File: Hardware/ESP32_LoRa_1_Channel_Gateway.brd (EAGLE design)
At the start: 25.4 x 45.7 mm, 86 parts, among them J3 USB, J4 QWIIC, J6 U.FL, Q1 MBT3904DW1T1, U1 3.3V, U2 CH340C, U3 ESP-WROOM-32NARROW, U4 RFM95W

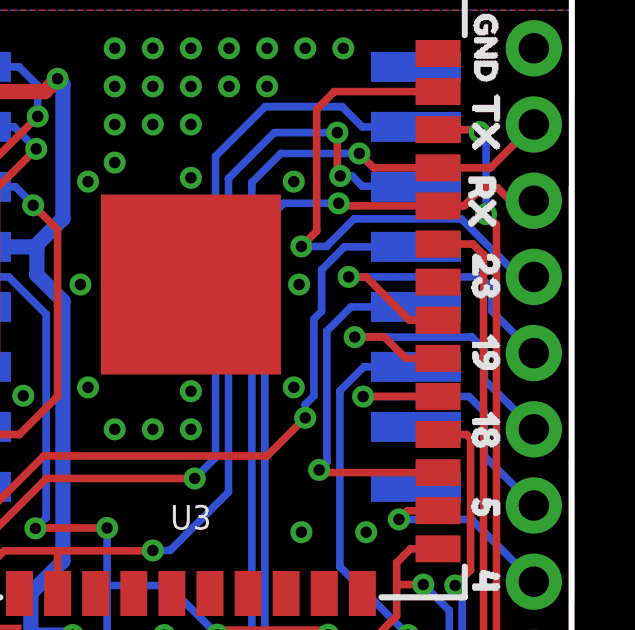
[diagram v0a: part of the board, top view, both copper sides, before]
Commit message: Moved CC atribution
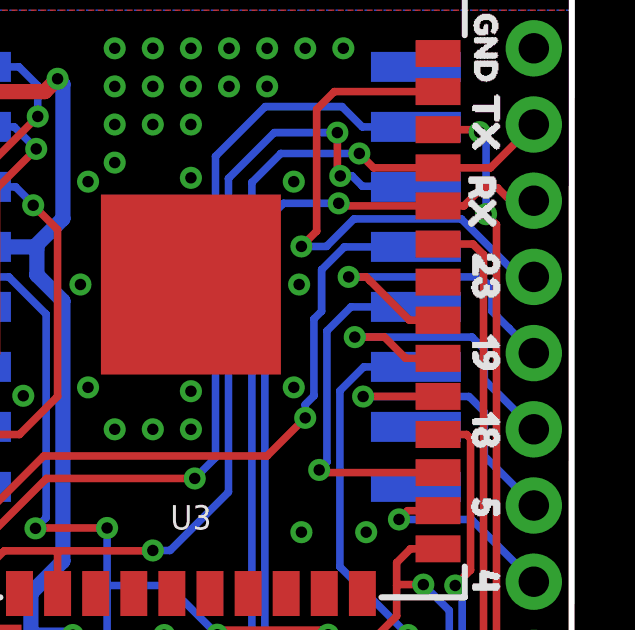
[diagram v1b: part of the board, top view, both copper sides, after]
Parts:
- moved FRAME1 7.83 mm to (-4.95, -9.91)
- moved LOGO2 7.65 mm to (6.48, -13.0)
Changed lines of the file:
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@@
 <hole x="1.27" y="17.78" drill="1.016"/>
 <text x="2.032" y="0.381" size="1.27" layer="16" font="vector" ratio="15" rot="MR0">v1</text>
-<text x="29.21" y="-7.62" size="1.778" layer="51" font="vector" ratio="15">Jim Lindblom</text>
-<text x="29.21" y="-11.43" size="1.778" layer="51" font="vector" ratio="15">Owen Lyke</text>
+<text x="22.479" y="-10.033" size="1.778" layer="51" font="vector" ratio="15">Jim Lindblom</text>
+<text x="22.352" y="-12.954" size="1.778" layer="51" font="vector" ratio="15">Owen Lyke</text>
 <dimension x1="27.94" y1="0" x2="27.94" y2="45.72" x3="30.48" y3="22.86" textsize="1.778" textratio="15" layer="47" unit="inch"/>
 <dimension x1="0" y1="48.26" x2="25.4" y2="48.26" x3="12.7" y3="50.8" textsize="1.778" textratio="15" layer="47" unit="inch"/>
@@
 <attribute name="VALUE" x="9.144" y="18.034" size="0.6096" layer="27" font="vector" ratio="20" rot="R180" align="top-center"/>
 </element>
-<element name="FRAME1" library="SparkFun-Aesthetics" package="CREATIVE_COMMONS" value="FRAME-LETTER" x="2.54" y="-7.62"/>
+<element name="FRAME1" library="SparkFun-Aesthetics" package="CREATIVE_COMMONS" value="FRAME-LETTER" x="-4.953" y="-9.906"/>
 <element name="Q1" library="esp32-thing-temp" package="SC70-6" value="MBT3904DW1T1" x="17.78" y="16.51" smashed="yes" rot="R90">
 <attribute name="NAME" x="16.383" y="16.51" size="0.6096" layer="25" font="vector" ratio="20" rot="R90" align="bottom-center"/>
@@
 <element name="U$45" library="buzzard_labels" package="ESP32_LORA_1#CH_GATEWAY23" value="" x="24.003" y="8.763" rot="MR0"/>
 <element name="LOGO1" library="SparkFun-Aesthetics" package="OSHW-LOGO-M" value="OSHW-LOGOM" x="22.606" y="2.54" rot="MR0"/>
-<element name="LOGO2" library="SparkFun-Aesthetics" package="REVISION" value="REVISION" x="13.97" y="-11.43"/>
+<element name="LOGO2" library="SparkFun-Aesthetics" package="REVISION" value="REVISION" x="6.477" y="-12.954"/>
 <element name="FD1" library="SparkFun-Aesthetics" package="FIDUCIAL-1X2" value="FIDUCIAL1X2" x="24.13" y="44.45"/>
 <element name="FD2" library="SparkFun-Aesthetics" package="FIDUCIAL-1X2" value="FIDUCIAL1X2" x="24.13" y="44.45" rot="MR0"/>
@@
 <wire x1="20.938" y1="29.036" x2="19.986" y2="29.036" width="0.254" layer="1"/>
 <wire x1="18.542" y1="30.48" x2="17.9578" y2="30.48" width="0.254" layer="1"/>
-<wire x1="19.986" y1="29.036" x2="18.542" y2="30.48" width="0.254" layer="1"/>
+<wire x1="19.986" y1="29.036" x2="18.669" y2="30.353" width="0.254" layer="1"/>
+<wire x1="18.669" y1="30.353" x2="18.542" y2="30.48" width="0.254" layer="1"/>
 <wire x1="22.352" y1="30.48" x2="22.733" y2="30.099" width="0.254" layer="16"/>
 <wire x1="22.733" y1="30.099" x2="22.733" y2="29.337" width="0.254" layer="16"/>
 <wire x1="17.9578" y1="30.48" x2="22.352" y2="30.48" width="0.254" layer="16"/>
-<wire x1="22.733" y1="29.337" x2="24.13" y2="27.94" width="0.254" layer="16"/>
+<wire x1="22.733" y1="29.337" x2="23.3045" y2="28.7655" width="0.254" layer="16"/>
+<wire x1="23.3045" y1="28.7655" x2="24.13" y2="27.94" width="0.254" layer="16"/>
 </signal>
 <signal name="IO18">

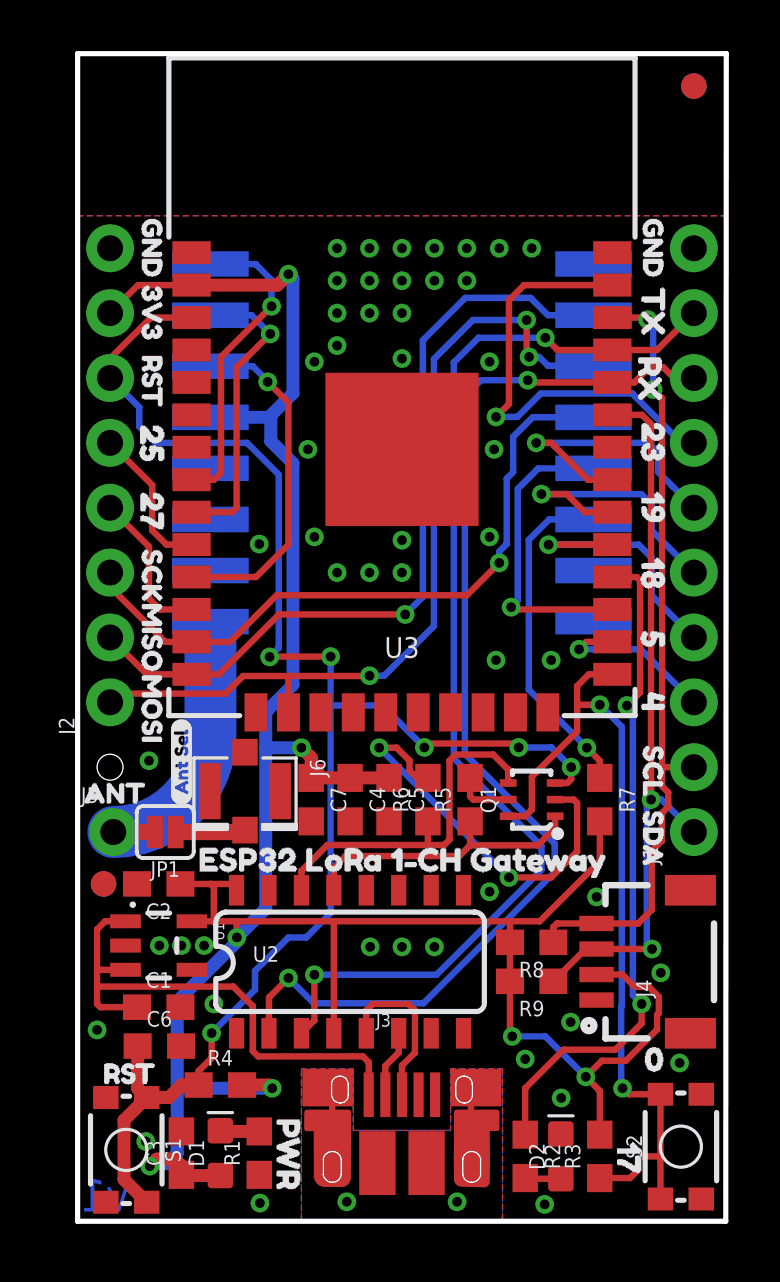
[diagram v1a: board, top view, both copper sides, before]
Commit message: Moved LEDs and silk
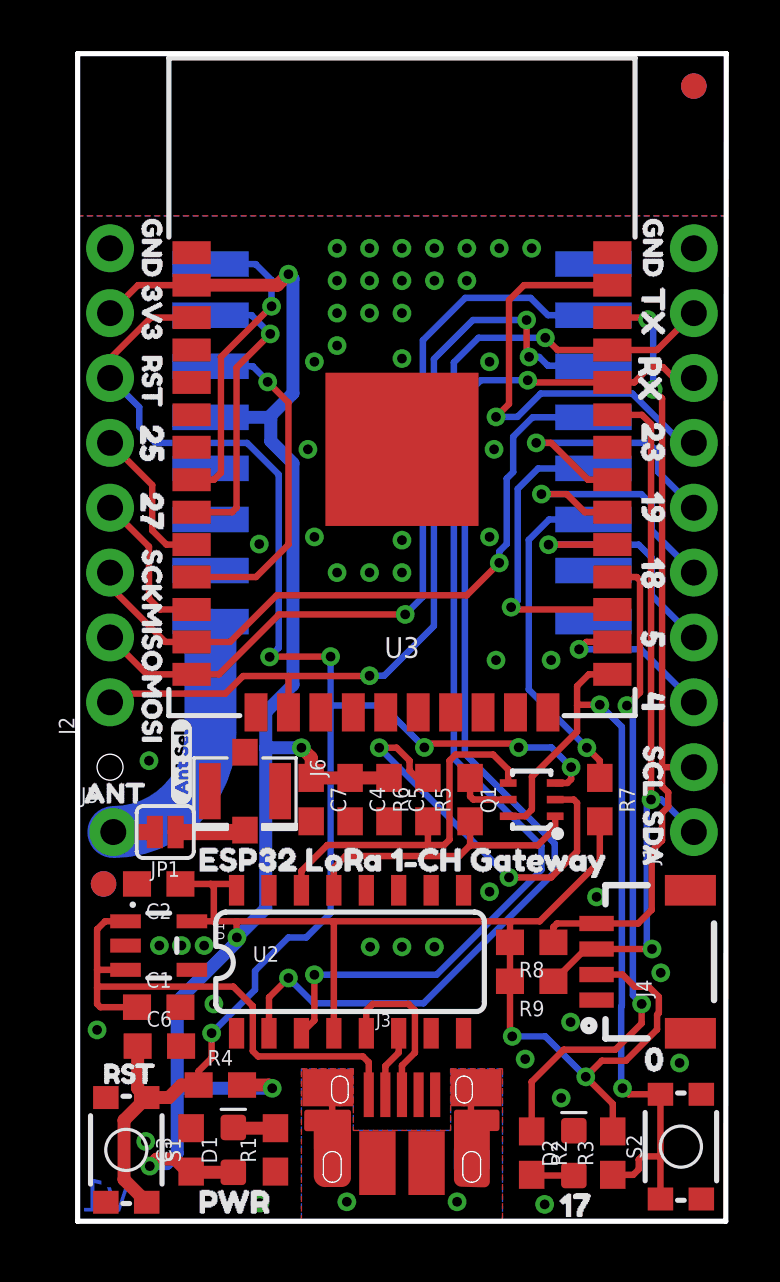
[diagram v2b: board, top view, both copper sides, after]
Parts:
- moved U$22 5.93 mm to (3.94, 0.76), turned to 0 degrees
- moved U$23 4.76 mm to (18.1, 0.64), turned to 0 degrees
- moved R1 0.65 mm to (7.75, 2.79)
- moved D2 0.52 mm to (19.4, 2.67)
- moved D1 0.52 mm to (6.10, 2.79)
- moved R3 0.52 mm to (21.0, 2.67)
- moved C3 0.40 mm to (4.45, 2.79)
- moved R2 0.28 mm to (17.8, 2.67)
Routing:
- net 0: track 33.1 -> 32.6 mm

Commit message: Some changes from design review
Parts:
- JP1: device SparkFun-Jumpers:SMT-JUMPER_2_NO_SILK -> SparkFun-Jumpers:SMT-JUMPER_2_NO_NO-SILK
- moved LOGO1 21.0 mm to (3.05, 10.3)
- moved U$45 5.08 mm to (23.9, 3.68)
- moved LOGO5 4.83 mm to (18.8, 5.08)
- moved R8 1.53 mm to (17.1, 9.53), turned to 270 degrees
- moved R9 0.90 mm to (18.7, 9.53), turned to 270 degrees
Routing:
- net 3.3V: track 109.0 -> 112.3 mm
- net TXO: track 45.0 -> 47.8 mm
- net RXI: track 45.2 -> 47.5 mm
- net SCL: track 31.1 -> 32.9 mm
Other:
- board text added: "v10"
- board text removed: "v1"

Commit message: Made small fixes
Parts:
- removed U$47: (no value), buzzard_labels (1):ANT_SEL0
- added U$24: (no value), buzzard_labels (1):U#FL0
- LOGO1: value OSHW-LOGOM -> OSHW-LOGOS; device SparkFun-Aesthetics:OSHW-LOGO-M -> SparkFun-Aesthetics:OSHW-LOGO-S
- moved LOGO1 0.51 mm to (2.54, 10.3)
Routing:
- net 3.3V: track 112.3 -> 106.2 mm
- net N$12: track 15.8 -> 15.2 mm

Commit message: Fixed checklist issues
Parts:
- removed LOGO5: SFE_LOGO_NAME_FLAME.1_INCH, SparkFun-Aesthetics:SFE_LOGO_NAME_FLAME_.1
- added LOGO3: OSHW-LOGOS, SparkFun-Aesthetics:OSHW-LOGO-S
- C2: value 1.0uF -> 0.1uF
- C4: value 0.1uF -> 1.0uF
- C6: value 0.1uF -> 4.7uF
- C7: value 4.7uF -> 0.1uF
- J1: value (none) -> USB; device SparkFun-Connectors:1X10_NO_SILK -> SparkFun-Connectors:USB-MICROB-PTH-MILL
- J2: value (none) -> U.FL; device SparkFun-Connectors:1X08_NO_SILK -> SparkFun-Connectors:U.FL
- J3: value USB -> (none); device SparkFun-Connectors:USB-MICROB-PTH-MILL -> SparkFun-Connectors:1X01_NO_SILK
- J4: value QWIIC -> (none); device SparkFun-Connectors:1X04_1MM_RA -> SparkFun-Connectors:1X08_NO_SILK
- J5: device SparkFun-Connectors:1X01_NO_SILK -> SparkFun-Connectors:1X10_NO_SILK
- J6: value U.FL -> QWIIC; device SparkFun-Connectors:U.FL -> SparkFun-Connectors:1X04_1MM_RA
- LOGO1: value OSHW-LOGOS -> REVISION; device SparkFun-Aesthetics:OSHW-LOGO-S -> SparkFun-Aesthetics:REVISION
- LOGO2: value REVISION -> SFE_LOGO_NAME_FLAME.1_INCH; device SparkFun-Aesthetics:REVISION -> SparkFun-Aesthetics:SFE_LOGO_NAME_FLAME_.1
- Q1: device esp32-thing-temp:SC70-6 -> SparkFun-DiscreteSemi:SC70-6
- R1: value 1k -> 10k
- R3: value 10k -> 1k
- R6: value 10k -> 2.2k
- R8: value 2.2k -> 10k
- U2: value CH340C -> ESP-WROOM-32NARROW; device SparkFun-IC-Comms:SO016 -> SparkFun-RF:ESP-WROOM-32-NARROW
- U3: value ESP-WROOM-32NARROW -> CH340C; device esp32_lora_gateway:ESP-WROOM-32-NARROW -> SparkFun-IC-Comms:SO016
- moved FD2 38.9 mm to (1.02, 13.2), flipped to the top
- moved FD3 38.9 mm to (24.1, 44.5)
- moved LOGO1 23.6 mm to (6.48, -13.0), flipped to the top
- moved J5 22.7 mm to (24.1, 15.2), turned to 90 degrees
- moved LOGO2 21.8 mm to (18.8, 5.08), flipped to the bottom
- moved J4 21.6 mm to (1.27, 20.3)
- moved U2 21.4 mm to (12.7, 31.5), turned to 90 degrees
- moved U3 21.4 mm to (10.7, 10.2), turned to 0 degrees
- moved R4 18.6 mm to (20.4, 16.5), turned to 270 degrees
- moved J1 15.4 mm to (12.7, 4.95), turned to 0 degrees
- moved J6 15.3 mm to (20.3, 10.2), turned to 90 degrees
- moved J3 15.3 mm to (1.40, 15.2)
- moved C3 15.1 mm to (10.7, 16.5), turned to 270 degrees
- moved R5 14.9 mm to (21.0, 2.67)
- moved C7 14.5 mm to (4.45, 2.79), turned to 90 degrees
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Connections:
- net !DTR: now also R7.1, U3.13; no longer R5.1, U2.13
- net !RTS: now also R8.1, U3.14; no longer R6.1, U2.14
- net 0: now also R5.1, U2.25; no longer R3.1, U3.25
- net 3.3V: now also C6.1, J4.7, J6.2, R1.2, R5.2, R6.2, U2.2, U3.16, U3.4; no longer C2.1, J2.7, J4.2, R3.2, R7.2, R8.2, U2.16, U2.4, U3.2
- net ANT: now also J3.1; no longer J5.1
- net D+: now also J1.D+, U3.5; no longer J3.D+, U2.5
- net D-: now also J1.D-, U3.6; no longer J3.D-, U2.6
- net GND: now also J1.GND, J2.1, J2.2, J4.8, J5.10, R2.1, U2.15, U2.38, U2.GND; no longer J1.10, J2.8, J3.GND, J4.1, J6.2, R1.1, U3.15, U3.38, U3.GND
- net IO17: now also R3.1, U2.28; no longer R2.1, U3.28
- net IO18: now also J5.5, U2.30; no longer J1.5, U3.30
- net IO19: now also J5.6, U2.31; no longer J1.6, U3.31
- net IO23: now also J5.7, U2.37; no longer J1.7, U3.37
- net IO25: now also J4.5, U2.10; no longer J2.5, U3.10
- net IO27: now also J4.4, U2.12; no longer J2.4, U3.12
- net IO4: now also J5.3, U2.26; no longer J1.3, U3.26
- net IO5: now also J5.4, U2.29; no longer J1.4, U3.29
- net MISO: now also J4.2, U2.14; no longer J2.2, U3.14
- net MOSI: now also J4.1, U2.16; no longer J2.1, U3.16
- net N$1: now also R2.2; no longer R1.2
- net N$10: now also R7.2; no longer R5.2
- net N$12: now also R8.2; no longer R6.2
- net N$2: now also R3.2; no longer R2.2
- net N$3: now also J2.FEED; no longer J6.FEED
- net RESET: now also C2.1, J4.6, R1.1, U2.3; no longer C6.1, J2.6, R4.1, U3.3
- net RFM_CS: now also U2.27; no longer U3.27
- net RFM_DIO1/33: now also U2.9; no longer U3.9
- net RFM_DIO2/32: now also U2.8; no longer U3.8
- net RFM_INT/26: now also U2.11; no longer U3.11
- net RFM_RST: now also R4.1; no longer R7.1
- net RXI: now also J5.8, U2.34, U3.2; no longer J1.8, U2.2, U3.34
- net SCK: now also J4.3, U2.13; no longer J2.3, U3.13
- net SCL: now also J5.2, J6.4, R9.1, U2.36; no longer J1.2, J4.4, R8.1, U3.36
- net SDA: now also J5.1, J6.3, R6.1, U2.33; no longer J1.1, J4.3, R9.1, U3.33
- net SHIELD: now also J1.SHIELD, J1.SHIELD10, J1.SHIELD2, J1.SHIELD3, J1.SHIELD4, J1.SHIELD5, J1.SHIELD6, J1.SHIELD7, J1.SHIELD8, J1.SHIELD9; no longer J3.SHIELD, J3.SHIELD10, J3.SHIELD2, J3.SHIELD3, J3.SHIELD4, J3.SHIELD5, J3.SHIELD6, J3.SHIELD7, J3.SHIELD8, J3.SHIELD9
- net TXO: now also J5.9, U2.35, U3.3; no longer J1.9, U2.3, U3.35
- net V_USB: now also J1.VBUS; no longer J3.VBUS
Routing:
- net V_USB: track 21.1 -> 15.8 mm
- net 3.3V: track 106.2 -> 109.8 mm
- net RESET: track 63.2 -> 62.3 mm
